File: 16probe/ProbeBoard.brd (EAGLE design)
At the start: 62.7 x 13 mm, 81 parts, among them Q1 2N7002, Q2 2N7002, U1 LTC2495CUHFPBF, U3 MAX6037AAUKADJ+T, U4 CSTCE16M0V53A-R0, U5 TPS79733DCKR, U6 ATMEGA328P_TQFPQFN_32

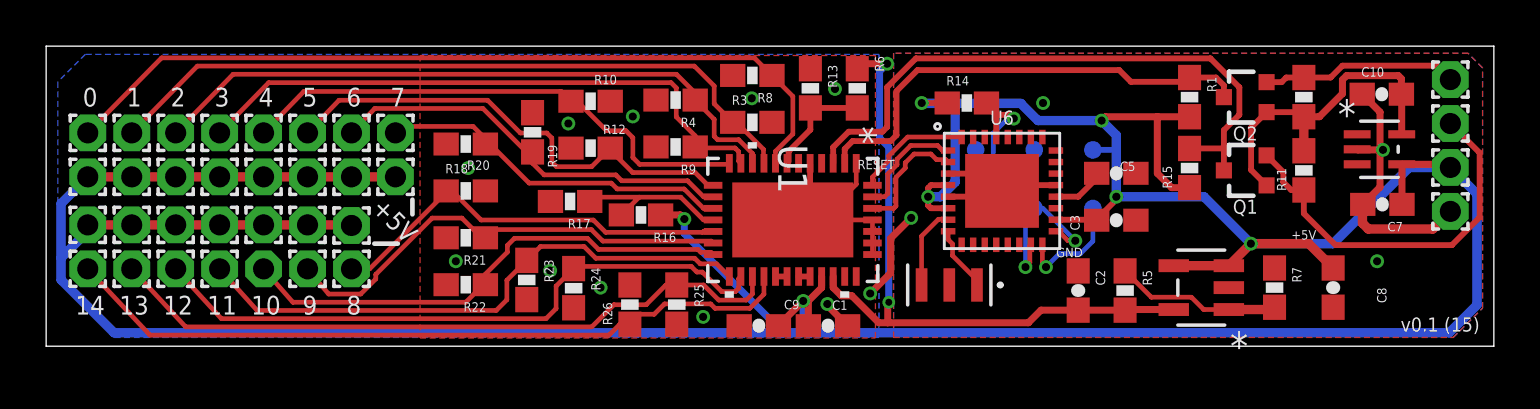
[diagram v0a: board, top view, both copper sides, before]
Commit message: switch out passives and crystal
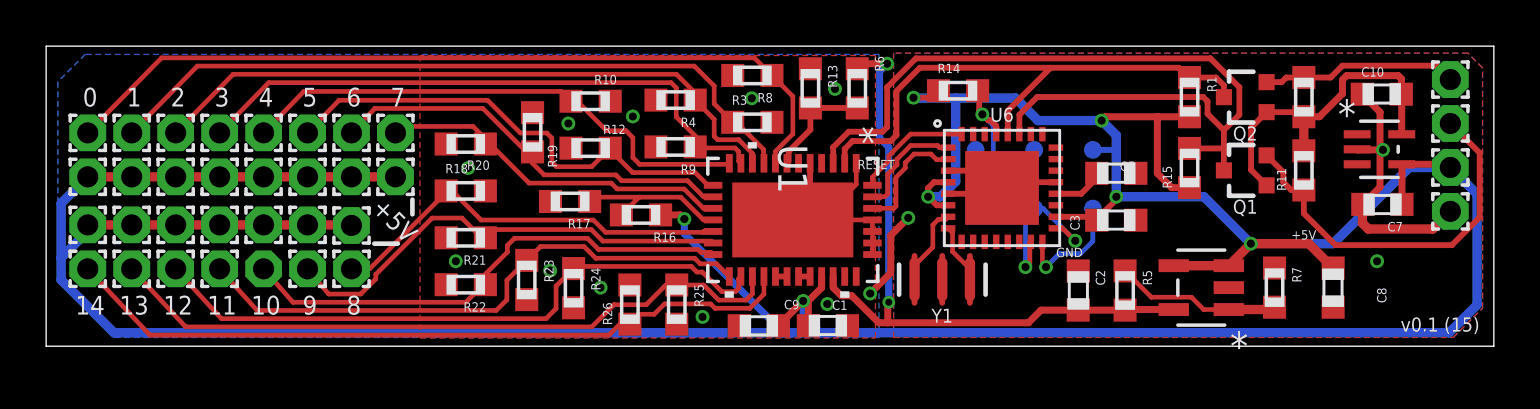
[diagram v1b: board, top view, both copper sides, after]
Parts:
- removed U4: CSTCE16M0V53A-R0, Murata Resonator:CSTCE_V
- added Y1: 8MHz, bschulz:RESONATOR-SMD-3.2X1.3
- C1, C10, C2, C3, C5, C7, C8, C9: device SparkFun:0603-CAP -> bschulz_passives:C0603
- R1, R10, R11, R12, R13, R14, R15, R16, R17, R18, R19, R2, R20, R21, R22, R23, R24, R25, R26, R3, R4, R5, R6, R7, R8, R9: device SparkFun:0603-RES -> bschulz_passives:R0603
- moved R14 0.66 mm to (39.5, 11.1)
- moved U6 0.13 mm to (41.4, 6.86)
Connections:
- net COM: now also Y1.2; no longer U4.2
- net N$1: now also Y1.3; no longer U4.3
- net N$7: now also Y1.1; no longer U4.1
- net SCL5V: now also U6.28
- net SDA5V: now also U6.27
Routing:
- net SDA5V: track 26.8 -> 37.8 mm
- net SCL5V: track 20.5 -> 24.1 mm
- net COM: track 40.7 -> 39.4 mm, vias 15 -> 14
- net +5V: track 175.2 -> 175.9 mm

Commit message: replace voltage reference IC
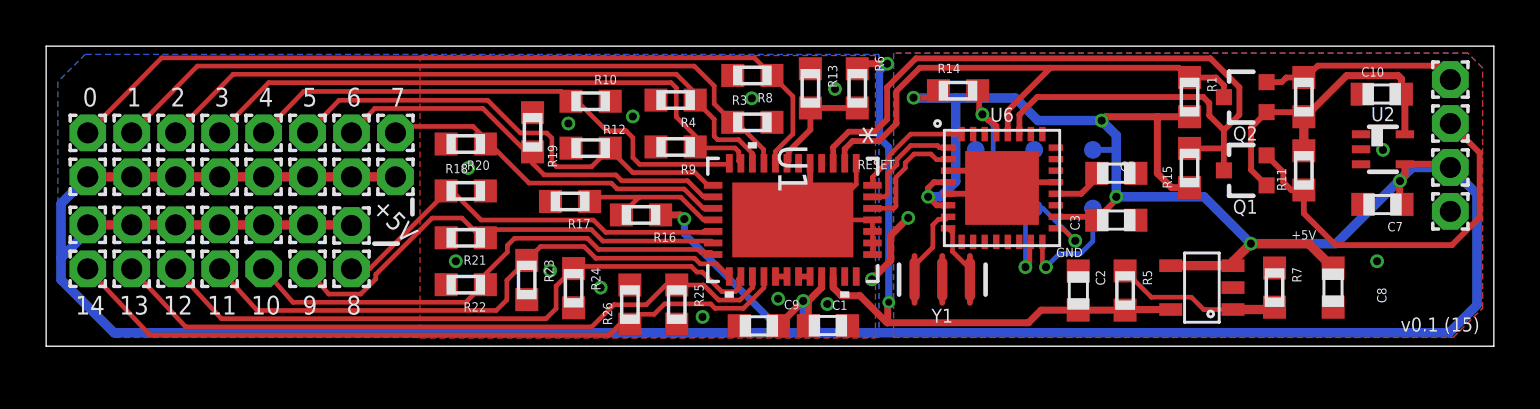
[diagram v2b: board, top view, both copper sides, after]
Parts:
- removed U5: TPS79733DCKR, TPS79733:DCK5
- added U2: TPS79733, bschulz:DCK_R-PDSO-G5
- U3: value MAX6037AAUKADJ+T -> MAX6037ADJSOT23; device MAX6037AAUKADJ:21-0057F -> bschulz:SOT23-5
- turned U3 to 90 degrees
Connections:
- net +5V: now also U2.4; no longer U5.4
- net 3.3V: now also U2.5; no longer U5.5
- net COM: now also U2.2; no longer U5.2
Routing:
- net COM: track 39.4 -> 27.2 mm, vias 14 -> 15
- net +5V: track 175.9 -> 176.1 mm, vias 7 -> 8

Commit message: shift SDA path
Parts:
- moved C10 0.63 mm to (57.9, 10.3)
- moved C7 0.51 mm to (57.9, 5.64)
- moved U2 0.51 mm to (57.9, 8.03)
- moved C8 0.51 mm to (55.3, 2.54)
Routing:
- net +5V: track 176.1 -> 172.0 mm, vias 8 -> 7
- net SDA3.3V: track 16.8 -> 15.0 mm
- net IO4: track 5.23 -> 4.37 mm
- net COM: vias 15 -> 16
